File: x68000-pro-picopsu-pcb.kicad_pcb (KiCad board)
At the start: 2 copper layers, 209 x 98 mm, 17 parts, among them J1 Fan Header, J2 Screw_Terminal_01x07, J3 Screw_Terminal_01x07, J4 PicoPSU, U1 74LS04

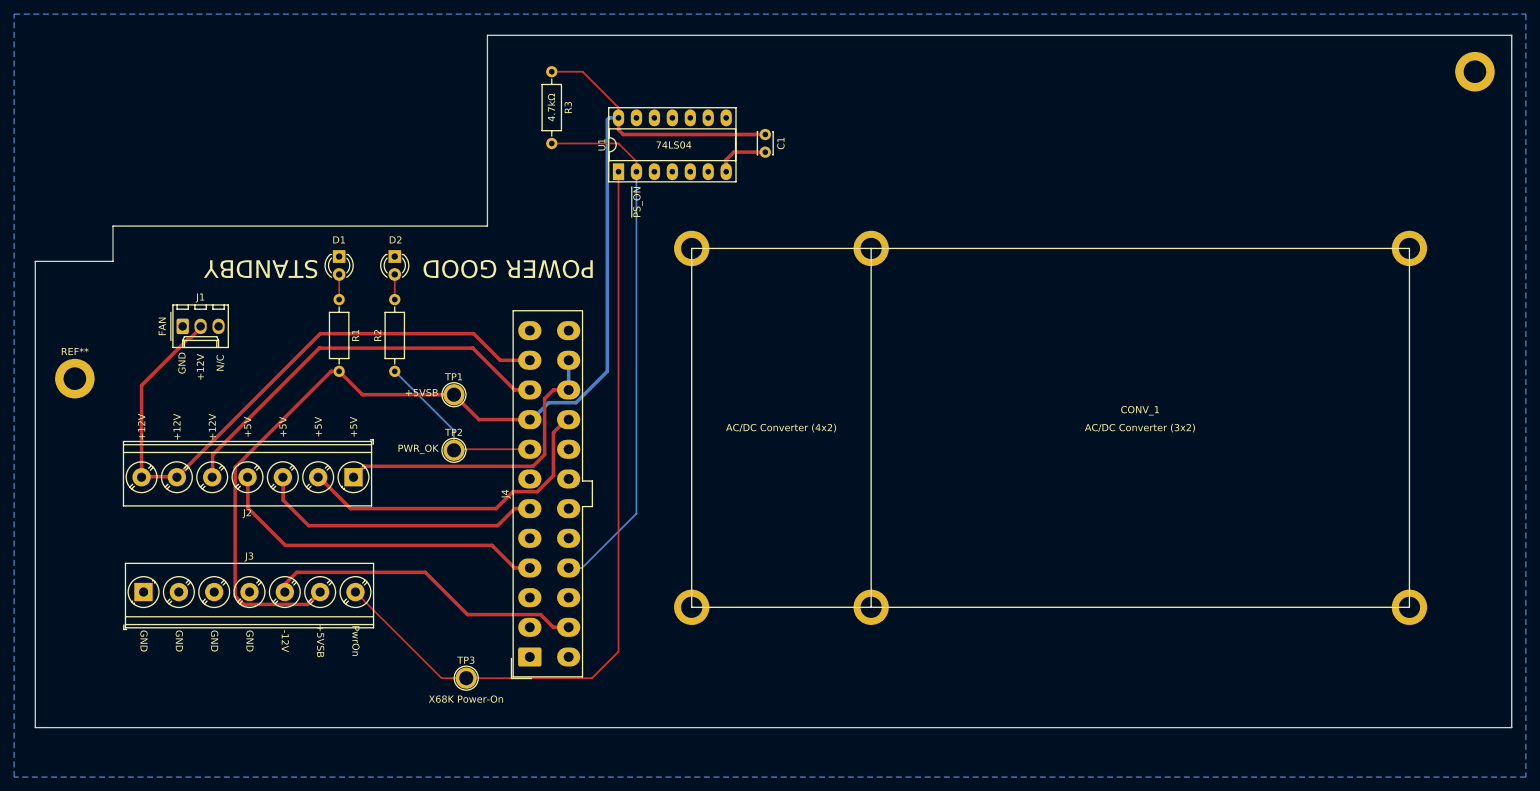
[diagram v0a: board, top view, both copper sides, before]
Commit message: Zones instead of thin traces
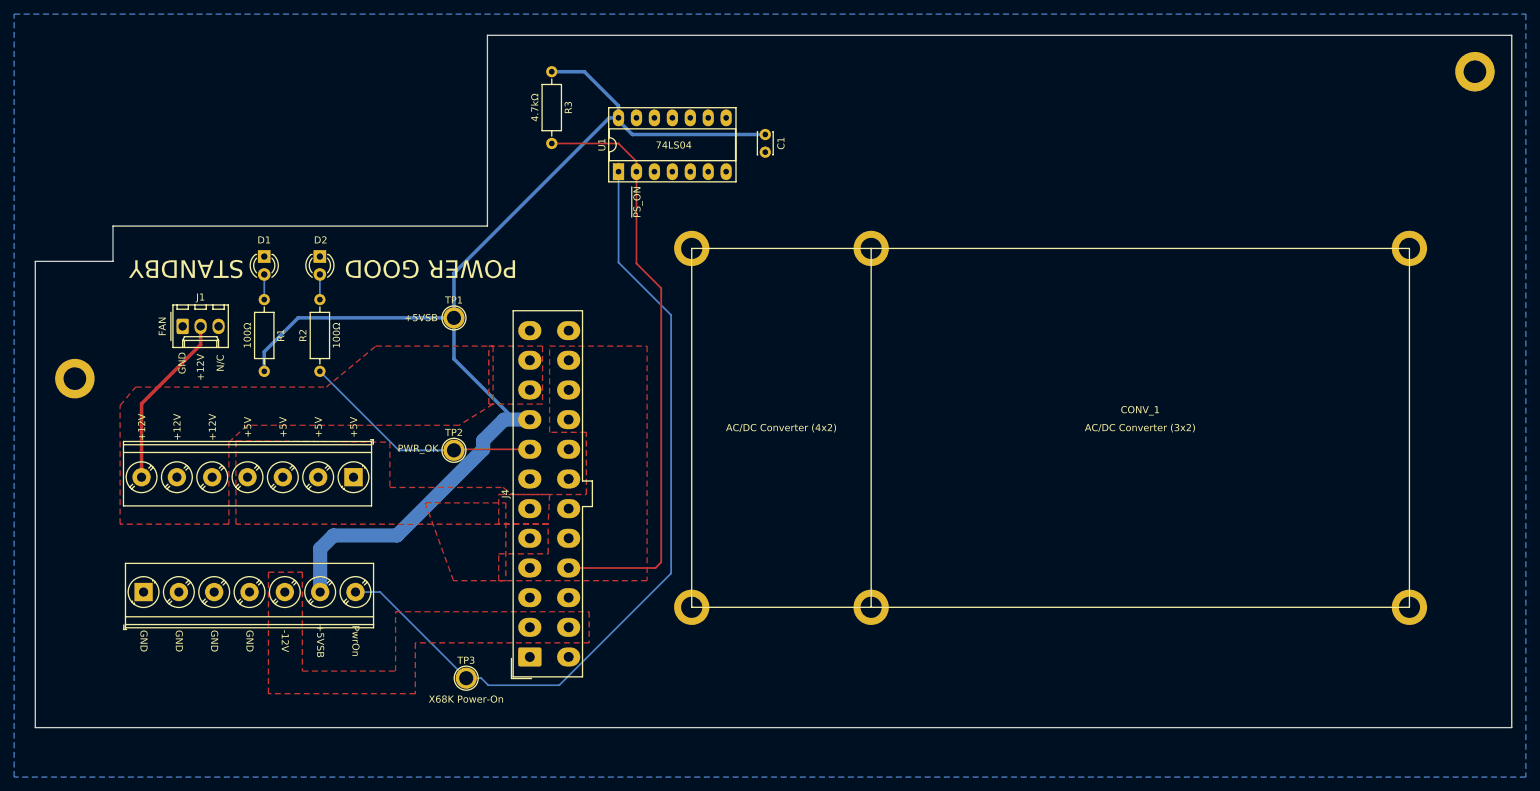
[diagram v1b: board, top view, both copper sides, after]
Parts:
- moved TP1 10.9 mm to (80.3, 92.0)
- moved D2 10.6 mm to (61.3, 83.3)
- moved R2 10.6 mm to (61.3, 99.6)
- moved D1 10.6 mm to (53.4, 83.3)
- moved R1 10.6 mm to (53.4, 89.4)
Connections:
- J1 pad 2: /PSU_12V_6 -> /PSU_12V
- J2 pad 2: /PSU_5V_2 -> /PSU_5V
- J2 pad 3: /PSU_5V_3 -> /PSU_5V
- J2 pad 4: /PSU_5V_4 -> /PSU_5V
- J2 pad 5: /PSU_12V_5 -> /PSU_12V
- J2 pad 6: /PSU_12V_6 -> /PSU_12V
- J2 pad 7: /PSU_12V_6 -> /PSU_12V
- J4 pad 10: /PSU_12V_5 -> /PSU_12V
- J4 pad 11: /PSU_12V_6 -> /PSU_12V
- J4 pad 21: /PSU_5V_2 -> /PSU_5V
- J4 pad 4: /PSU_5V_4 -> /PSU_5V
- J4 pad 6: /PSU_5V_3 -> /PSU_5V
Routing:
- net /PSU_12V_6: track 89.8 -> 0.00 mm
- net /PSU_12V_5: track 56.7 -> 0.00 mm
- net /PSU_5V_4: track 47.9 -> 0.00 mm
- net /PSU_5V_2: track 46.0 -> 0.00 mm
- net /PSU_NEG_12V: track 45.1 -> 0.30 mm
- net /PSU_5V: track 44.3 -> 0.00 mm
- net /PSU_5V_3: track 40.7 -> 0.00 mm
- net /PSU_12V: track 0.00 -> 24.8 mm
- net /~PS_ON: track 75.7 -> 84.7 mm
- net /PWR_OK: track 25.8 -> 34.6 mm
- net /PSU_COM: track 7.68 -> 0.00 mm
- net /POWER_ON_REQUEST: track 111.8 -> 118.9 mm
- net /PSU_5V_STANDBY: track 168.5 -> 169.7 mm
- added copper zone on F.Cu, net /PSU_12V
- added copper zone on F.Cu, net /PSU_5V
- added copper zone on F.Cu, net /PSU_NEG_12V
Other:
- board text removed: "4.7kΩ"

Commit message: Giant obnoxious logos
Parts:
- added G***: LOGO, logos:x68000-200dpi, F.Cu at (174.8, 62.2)
- added G***: LOGO, logos:leaded-solder-logo-800dpi, F.Cu at (226.4, 138.4)
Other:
- board text added: "PRO PicoPSU board"
- board text added: "version 0.1, leadedsolder.com 2021"

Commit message: Everything except central mounting hole
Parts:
- moved CONV_1 7.90 mm to (142.0, 140.4)
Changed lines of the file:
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@@
     (add_net "Net-(J4-Pad20)")
   )
-  (module logos:x68000-200dpi (layer F.Cu)
+  (module logos:x68000-200dpi locked (layer F.Cu)
     (at 174.8 62.2)
     (fp_text reference G*** (at 0 0) (layer F.SilkS) hide
@@
       (xy -34.096468 0.736723)) (layer F.SilkS) (width 0.01))
   )
-  (module logos:leaded-solder-logo-800dpi (layer F.Cu)
+  (module logos:leaded-solder-logo-800dpi locked (layer F.Cu)
     (at 226.4 138.4 90)
     (fp_text reference G*** (at 0 0 90) (layer F.SilkS) hide
@@
   )
   (module OffboardACDC:3x2_4x2 (layer F.Cu)
-    (at 139.319 132.969 180)
+    (at 142 140.4 180)
     (fp_text reference CONV_1 (at -38.1 27.94) (layer F.SilkS)
       (effects (font (size 1 1) (thickness 0.15)))

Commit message: Central mounting/support hole, in m3
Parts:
- added REF**: MountingHole_3.2mm_M3, MountingHole:MountingHole_3.2mm_M3, F.Cu at (163.0, 99.0)
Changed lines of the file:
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@@
   (general
     (thickness 1.6)
-    (drawings 39)
+    (drawings 41)
     (tracks 51)
     (zones 0)
-    (modules 19)
+    (modules 20)
     (nets 17)
   )
@@
     (add_net "Net-(J4-Pad2)")
     (add_net "Net-(J4-Pad20)")
+  )
+  (module MountingHole:MountingHole_3.2mm_M3 locked (layer F.Cu)
+    (at 163 99)
+    (descr "Mounting Hole 3.2mm, no annular, M3")
+    (tags "mounting hole 3.2mm no annular m3")
+    (attr virtual)
+    (fp_text reference REF** (at 0 -4.2) (layer F.SilkS) hide
+      (effects (font (size 1 1) (thickness 0.15)))
+    )
+    (fp_text value MountingHole_3.2mm_M3 (at 0 4.2) (layer F.Fab)
+      (effects (font (size 1 1) (thickness 0.15)))
+    )
+    (fp_circle (center 0 0) (end 3.45 0) (layer F.CrtYd) (width 0.05))
+    (fp_circle (center 0 0) (end 3.2 0) (layer Cmts.User) (width 0.15))
+    (fp_text user %R (at 0.3 0) (layer F.Fab)
+      (effects (font (size 1 1) (thickness 0.15)))
+    )
+    (pad 1 np_thru_hole circle (at 0 0) (size 3.2 3.2) (drill 3.2) (layers *.Cu *.Mask))
   )
   (module logos:x68000-200dpi locked (layer F.Cu)
@@
     )
   )
+  (dimension 51 (width 0.12) (layer Dwgs.User)
+    (gr_text "51.000 mm" (at 270.27 124.5 90) (layer Dwgs.User)
+      (effects (font (size 1 1) (thickness 0.15)))
+    )
+    (feature1 (pts (xy 163 99) (xy 269.586421 99)))
+    (feature2 (pts (xy 163 150) (xy 269.586421 150)))
+    (crossbar (pts (xy 269 150) (xy 269 99)))
+    (arrow1a (pts (xy 269 99) (xy 269.586421 100.126504)))
+    (arrow1b (pts (xy 269 99) (xy 268.413579 100.126504)))
+    (arrow2a (pts (xy 269 150) (xy 269.586421 148.873496)))
+    (arrow2b (pts (xy 269 150) (xy 268.413579 148.873496)))
+  )
+  (dimension 67 (width 0.12) (layer Dwgs.User)
+    (gr_text "67.000 mm" (at 196.5 173.27) (layer Dwgs.User)
+      (effects (font (size 1 1) (thickness 0.15)))
+    )
+    (feature1 (pts (xy 163 99) (xy 163 172.586421)))
+    (feature2 (pts (xy 230 99) (xy 230 172.586421)))
+    (crossbar (pts (xy 230 172) (xy 163 172)))
+    (arrow1a (pts (xy 163 172) (xy 164.126504 171.413579)))
+    (arrow1b (pts (xy 163 172) (xy 164.126504 172.586421)))
+    (arrow2a (pts (xy 230 172) (xy 228.873496 171.413579)))
+    (arrow2b (pts (xy 230 172) (xy 228.873496 172.586421)))
+  )
   (gr_text "PRO PicoPSU board" (at 195.6 70.4) (layer F.SilkS)

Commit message: Small fiddling
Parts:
- moved CONV_1 2.40 mm to (142.0, 138.0)
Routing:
- net /POWER_ON_REQUEST: track 118.9 -> 122.6 mm
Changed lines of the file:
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@@
   )
   (module OffboardACDC:3x2_4x2 (layer F.Cu)
-    (at 142 140.4 180)
+    (at 142 138 180)
     (fp_text reference CONV_1 (at -38.1 27.94) (layer F.SilkS)
       (effects (font (size 1 1) (thickness 0.15)))
@@
     (descr "Molex Mini-Fit Jr. Power Connectors, old mpn/engineering number: 5566-24A, example for new mpn: 39-28-x24x, 12 Pins per row, Mounting:  (http://www.molex.com/pdm_docs/sd/039281043_sd.pdf), generated with kicad-footprint-generator")
     (tags "connector Molex Mini-Fit_Jr side entry")
-    (fp_text reference J4 (at 23.1 -3.45 90) (layer F.SilkS)
+    (fp_text reference J4 (at 23.1 -3.45 90) (layer F.SilkS) hide
       (effects (font (size 1 1) (thickness 0.15)))
     )
@@
     (tags "test point plated hole")
     (attr virtual)
-    (fp_text reference TP2 (at 0 -2.498) (layer F.SilkS)
+    (fp_text reference TP2 (at 0 -2.498) (layer F.SilkS) hide
       (effects (font (size 1 1) (thickness 0.15)))
     )
@@
     (tags "test point plated hole")
     (attr virtual)
-    (fp_text reference TP1 (at 0 -2.498) (layer F.SilkS)
+    (fp_text reference TP1 (at 0 -2.498) (layer F.SilkS) hide
       (effects (font (size 1 1) (thickness 0.15)))
     )
@@
     (descr "Molex KK-254 Interconnect System, old/engineering part number: AE-6410-03A example for new part number: 22-27-2031, 3 Pins (http://www.molex.com/pdm_docs/sd/022272021_sd.pdf), generated with kicad-footprint-generator")
     (tags "connector Molex KK-254 side entry")
-    (fp_text reference J1 (at 2.54 -4.12) (layer F.SilkS)
+    (fp_text reference J1 (at 2.54 -4.12) (layer F.SilkS) hide
       (effects (font (size 1 1) (thickness 0.15)))
     )
@@
   (segment (start 69.81 130.81) (end 82 143) (width 0.25) (layer B.Cu) (net 15) (status 20))
   (segment (start 66.322 130.81) (end 69.81 130.81) (width 0.25) (layer B.Cu) (net 15) (status 10))
-  (segment (start 103.557 70.157) (end 103.557 71.302) (width 0.25) (layer B.Cu) (net 15) (status 30))
-  (segment (start 85.12132 144) (end 95.168821 144) (width 0.25) (layer B.Cu) (net 15))
-  (segment (start 95.168821 144) (end 111 128.168821) (width 0.25) (layer B.Cu) (net 15))
+  (segment (start 103.557 70.157) (end 103.557 71.302) (width 0.25) (layer B.Cu) (net 15))
+  (segment (start 103.557 84.157) (end 103.557 70.157) (width 0.25) (layer B.Cu) (net 15))
+  (segment (start 111 91.6) (end 103.557 84.157) (width 0.25) (layer B.Cu) (net 15))
+  (segment (start 82 143) (end 84.12132 143) (width 0.25) (layer B.Cu) (net 15))
+  (segment (start 111 128.168821) (end 111 91.6) (width 0.25) (layer B.Cu) (net 15))
+  (segment (start 103.886 144.018) (end 111 128.168821) (width 0.25) (layer B.Cu) (net 15))
+  (segment (start 85.12132 144) (end 103.886 144.018) (width 0.25) (layer B.Cu) (net 15))
   (segment (start 84.12132 143) (end 85.12132 144) (width 0.25) (layer B.Cu) (net 15))
-  (segment (start 111 128.168821) (end 111 91.6) (width 0.25) (layer B.Cu) (net 15))
-  (segment (start 103.557 84.157) (end 103.557 70.157) (width 0.25) (layer B.Cu) (net 15) (status 20))
-  (segment (start 111 91.6) (end 103.557 84.157) (width 0.25) (layer B.Cu) (net 15))
-  (segment (start 82 143) (end 84.12132 143) (width 0.25) (layer B.Cu) (net 15) (status 10))
   (segment (start 36.04 114.554) (end 36.04 104.16) (width 0.5) (layer F.Cu) (net 16) (status 10))
   (segment (start 44.4 95.8) (end 44.4 93.2) (width 0.5) (layer F.Cu) (net 16) (status 20))

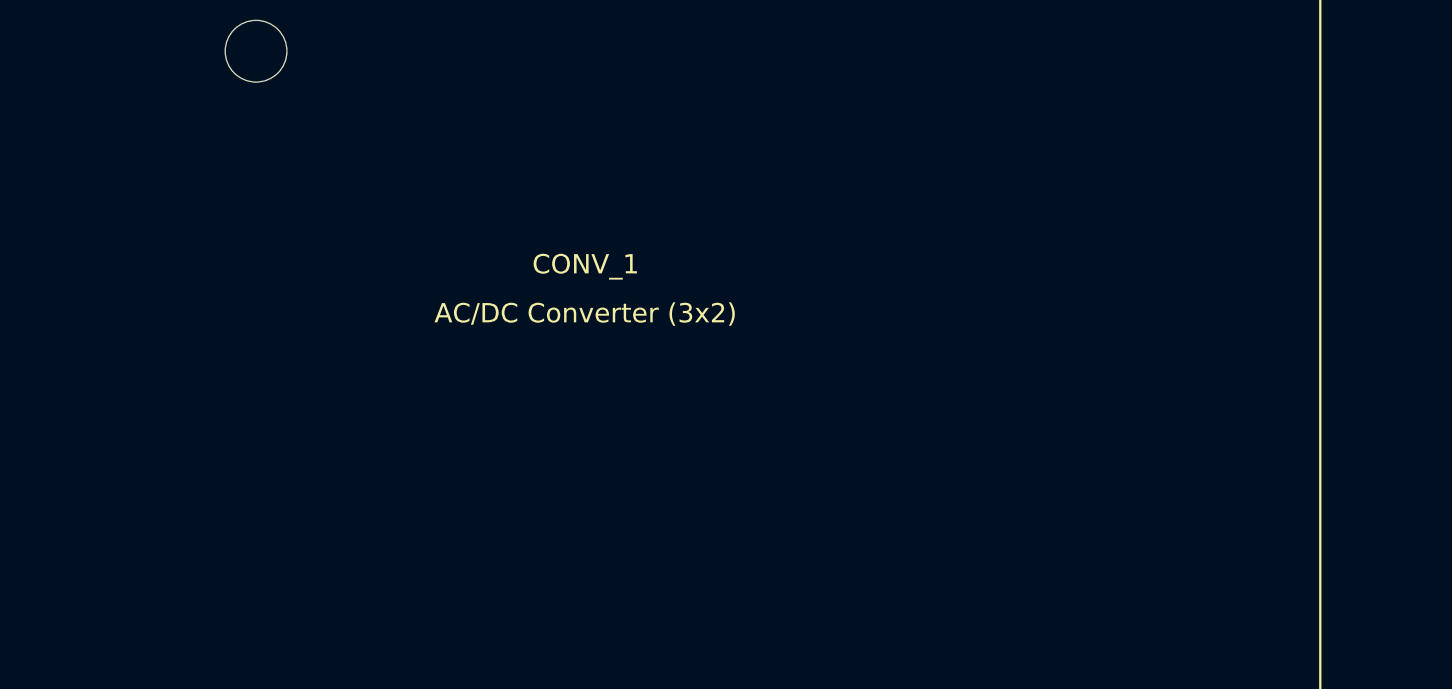
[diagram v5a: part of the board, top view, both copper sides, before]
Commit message: Bonus mounting hole
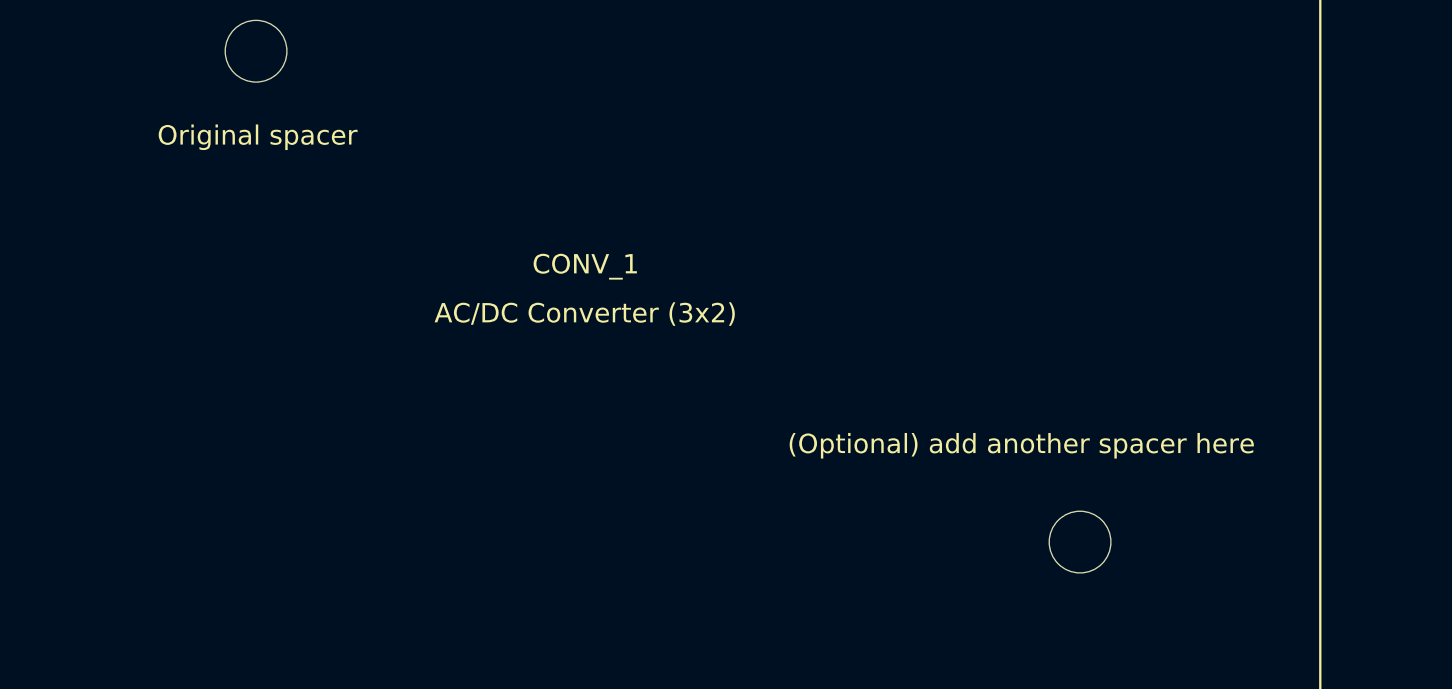
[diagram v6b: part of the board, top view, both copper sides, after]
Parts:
- added REF**: MountingHole_3.2mm_M3, MountingHole:MountingHole_3.2mm_M3, F.Cu at (205.7, 124.5)
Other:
- board text added: "(Optional) add another spacer here"
- board text added: "Original spacer"
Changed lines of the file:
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@@
   (general
     (thickness 1.6)
-    (drawings 41)
+    (drawings 43)
     (tracks 51)
     (zones 0)
-    (modules 20)
+    (modules 21)
     (nets 17)
   )
@@
       (outputformat 1)
       (mirror false)
-      (drillshape 1)
+      (drillshape 0)
       (scaleselection 1)
-      (outputdirectory ""))
+      (outputdirectory "plot"))
   )
   (net 0 "")
@@
     (add_net "Net-(J4-Pad2)")
     (add_net "Net-(J4-Pad20)")
+  )
+  (module MountingHole:MountingHole_3.2mm_M3 locked (layer F.Cu)
+    (at 205.74 124.46)
+    (descr "Mounting Hole 3.2mm, no annular, M3")
+    (tags "mounting hole 3.2mm no annular m3")
+    (attr virtual)
+    (fp_text reference REF** (at 0 -4.2) (layer F.SilkS) hide
+      (effects (font (size 1 1) (thickness 0.15)))
+    )
+    (fp_text value MountingHole_3.2mm_M3 (at 0 4.2) (layer F.Fab)
+      (effects (font (size 1 1) (thickness 0.15)))
+    )
+    (fp_text user %R (at 0.3 0) (layer F.Fab)
+      (effects (font (size 1 1) (thickness 0.15)))
+    )
+    (fp_circle (center 0 0) (end 3.2 0) (layer Cmts.User) (width 0.15))
+    (fp_circle (center 0 0) (end 3.45 0) (layer F.CrtYd) (width 0.05))
+    (pad 1 np_thru_hole circle (at 0 0) (size 3.2 3.2) (drill 3.2) (layers *.Cu *.Mask))
   )
   (module MountingHole:MountingHole_3.2mm_M3 locked (layer F.Cu)
@@
     )
   )
+  (gr_text "Original spacer" (at 163.068 103.378) (layer F.SilkS)
+    (effects (font (size 1 1) (thickness 0.15)))
+  )
+  (gr_text "(Optional) add another spacer here" (at 202.692 119.38) (layer F.SilkS)
+    (effects (font (size 1 1) (thickness 0.15)))
+  )
   (dimension 51 (width 0.12) (layer Dwgs.User)
